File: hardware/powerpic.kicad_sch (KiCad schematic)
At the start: 20 parts, among them U1 PIC16LF1919x-I/MR

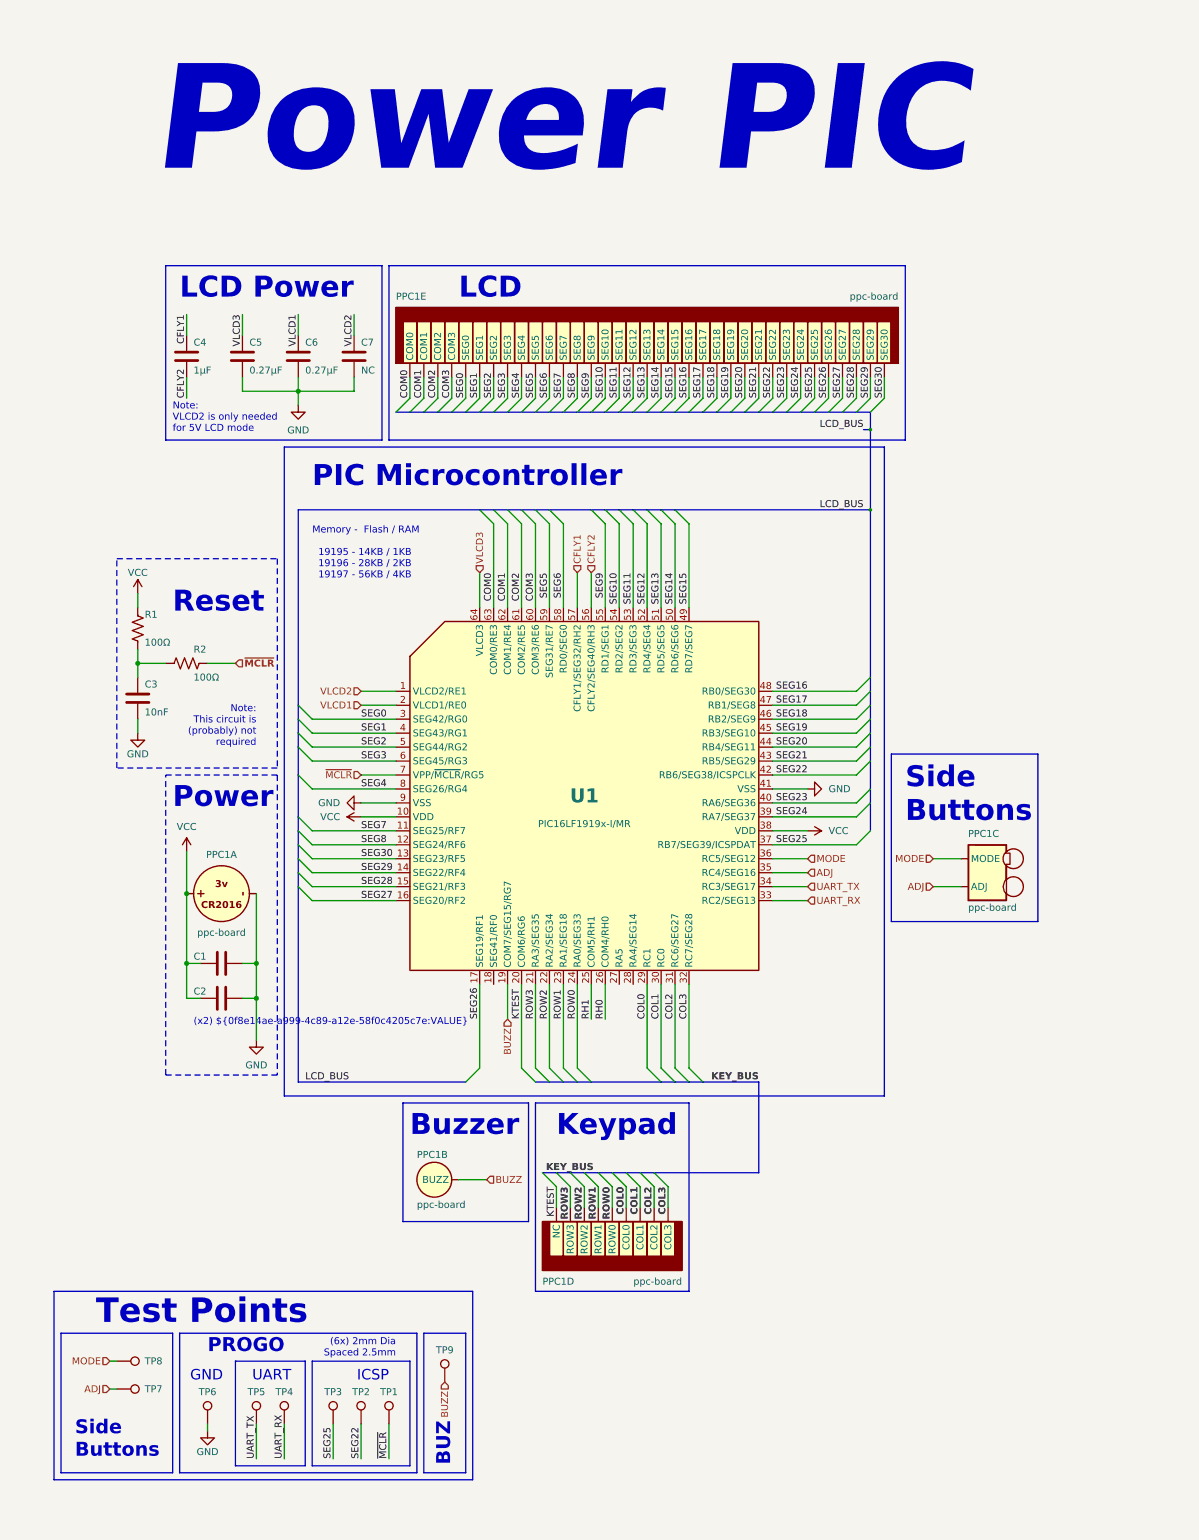
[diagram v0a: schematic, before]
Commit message: Redesigned board with RTCXTAL and led backlight
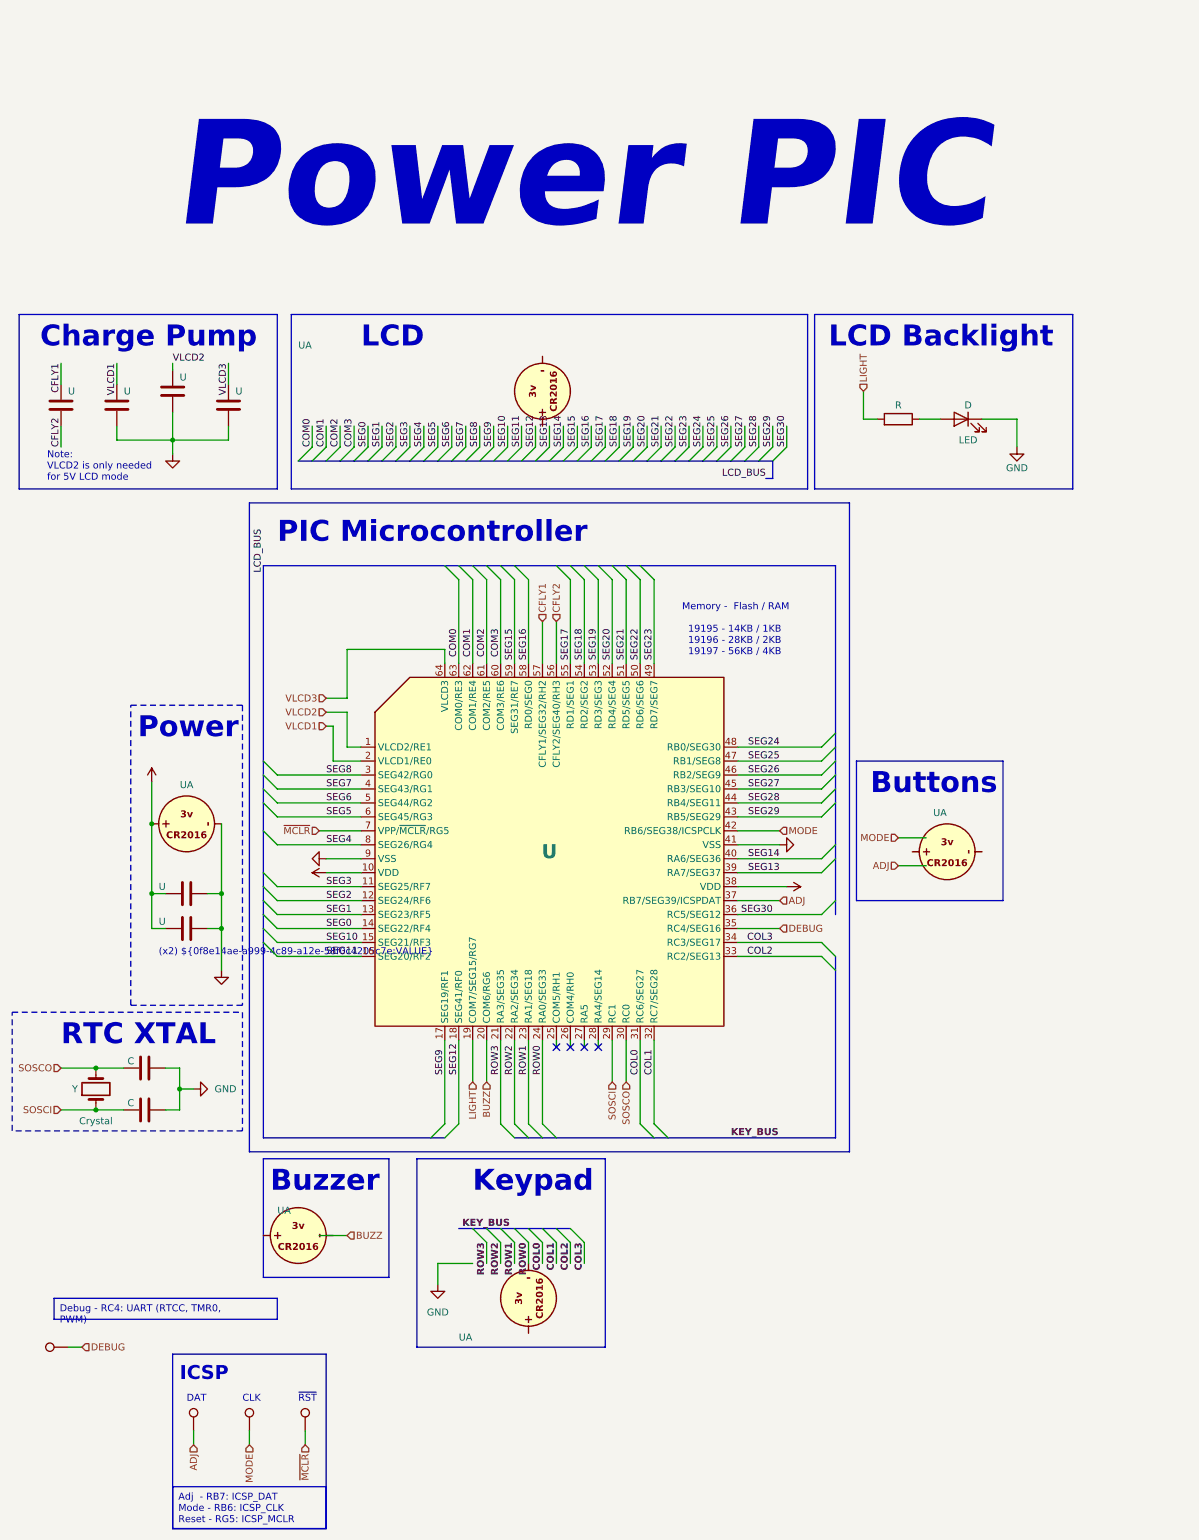
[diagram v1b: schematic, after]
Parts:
- removed C3: 10nF, Capacitor_SMD:C_0402_1005Metric, symbol Device:C
- removed R1, R2: 100Ω, Resistor_SMD:R_0402_1005Metric, symbol Device:R_US
- removed TP1: ~{MCLR}, powerpic:Progo_Pad_D2.0mm, symbol Connector:TestPoint
- removed TP2: ICSP_CLK, powerpic:Progo_Pad_D2.0mm, symbol Connector:TestPoint
- removed TP3: ICSP_DAT, powerpic:Progo_Pad_D2.0mm, symbol Connector:TestPoint
- removed TP4: UART_RX, powerpic:Progo_Pad_D2.0mm, symbol Connector:TestPoint
- removed TP5: UART_TX, powerpic:Progo_Pad_D2.0mm, symbol Connector:TestPoint
- removed TP6: GND, powerpic:Progo_Pad_D2.0mm, symbol Connector:TestPoint
- removed TP7: ADJ, powerpic:Progo_Pad_D2.0mm, symbol Connector:TestPoint
- removed TP8: MODE, powerpic:Progo_Pad_D2.0mm, symbol Connector:TestPoint
- removed TP9: BUZZ, powerpic:Progo_Pad_D2.0mm, symbol Connector:TestPoint
- added C (x2): C, symbol Device:C
- added D: LED, symbol Device:LED
- added R: R, symbol Device:R
- added TP (x4): TestPoint, symbol Connector:TestPoint
- added Y: Crystal, symbol Device:Crystal
- U: renamed from C5; value 0.27μF -> (none); footprint Capacitor_SMD:C_0402_1005Metric -> (none)
- U: renamed from C1; value 0.1μF -> (none); footprint Capacitor_SMD:C_0402_1005Metric -> (none)
- U: renamed from PPC1; value ppc-board -> (none); footprint powerpic:ppc-board -> (none)
- U: renamed from C4; value 1μF -> (none); footprint Capacitor_SMD:C_0402_1005Metric -> (none)
- U: renamed from U1; value PIC16LF1919x-I/MR -> (none); footprint Package_DFN_QFN:QFN-64-1EP_9x9mm_P0.5mm_EP5.4x5.4mm -> (none)
- U: renamed from C7; value NC -> (none); footprint Capacitor_SMD:C_0402_1005Metric -> (none)
- U: renamed from C6; value 0.27μF -> (none); footprint Capacitor_SMD:C_0402_1005Metric -> (none)
- U: renamed from C2; value 0.1μF -> (none); footprint Capacitor_SMD:C_0402_1005Metric -> (none)
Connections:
- net UART_RX is gone; now on net COL2: U.33 (RC2/SEG13)
- net UART_TX is gone; now on net COL3: U.34 (RC3/SEG17)
- net ADJ: now also U.37 (RB7/SEG39/ICSPDAT), TP.1; no longer U.35 (RC4/SEG16), U.5 (ADJ)
- net BUZZ: now also U.20 (COM6/RG6); no longer U.19 (COM7/SEG15/RG7), U.3 (BUZZ)
- net COL0: now also U.31 (RC6/SEG27); no longer U.11 (COL0), U.29 (RC1)
- net COL1: now also U.32 (RC7/SEG28); no longer U.12 (COL1), U.30 (RC0)
- net COL2: no longer U.13 (COL2), U.31 (RC6/SEG27)
- net COL3: no longer U.14 (COL3), U.32 (RC7/SEG28)
- net COM0: no longer U.15 (COM0)
- net COM1: no longer U.16 (COM1)
- net COM2: no longer U.17 (COM2)
- net COM3: no longer U.18 (COM3)
- net GND: now also C.2, C.2, D.1 (K)
- net MODE: now also U.42 (RB6/SEG38/ICSPCLK), TP.1; no longer U.36 (RC5/SEG12), U.4 (MODE)
- net ROW0: now also U.2 (GND); no longer U.10 (ROW0)
- net ROW1: no longer U.9 (ROW1)
- net ROW2: no longer U.8 (ROW2)
- net ROW3: no longer U.7 (ROW3)
- net SEG0: now also U.14 (SEG22/RF4); no longer U.19 (SEG0), U.3 (SEG42/RG0)
- net SEG1: now also U.13 (SEG23/RF5); no longer U.20 (SEG1), U.4 (SEG43/RG1)
- net SEG10: now also U.15 (SEG21/RF3); no longer U.29 (SEG10), U.54 (RD2/SEG2)
- net SEG11: now also U.16 (SEG20/RF2); no longer U.30 (SEG11), U.53 (RD3/SEG3)
- net SEG12: now also U.18 (SEG41/RF0); no longer U.31 (SEG12), U.52 (RD4/SEG4)
- net SEG13: now also U.39 (RA7/SEG37); no longer U.32 (SEG13), U.51 (RD5/SEG5)
- net SEG14: now also U.40 (RA6/SEG36); no longer U.33 (SEG14), U.50 (RD6/SEG6)
- net SEG15: now also U.59 (SEG31/RE7); no longer U.34 (SEG15), U.49 (RD7/SEG7)
- net SEG16: now also U.58 (RD0/SEG0); no longer U.35 (SEG16), U.48 (RB0/SEG30)
- net SEG17: now also U.55 (RD1/SEG1); no longer U.36 (SEG17), U.47 (RB1/SEG8)
- net SEG18: now also U.54 (RD2/SEG2); no longer U.37 (SEG18), U.46 (RB2/SEG9)
- net SEG19: now also U.53 (RD3/SEG3); no longer U.38 (SEG19), U.45 (RB3/SEG10)
- net SEG2: now also U.12 (SEG24/RF6); no longer U.21 (SEG2), U.5 (SEG44/RG2)
- net SEG20: now also U.52 (RD4/SEG4); no longer U.39 (SEG20), U.44 (RB4/SEG11)
- net SEG21: now also U.51 (RD5/SEG5); no longer U.40 (SEG21), U.43 (RB5/SEG29)
- net SEG22: now also U.50 (RD6/SEG6); no longer U.41 (SEG22), U.42 (RB6/SEG38/ICSPCLK)
- net SEG23: now also U.49 (RD7/SEG7); no longer U.40 (RA6/SEG36), U.42 (SEG23)
- net SEG24: now also U.48 (RB0/SEG30); no longer U.39 (RA7/SEG37), U.43 (SEG24)
- net SEG25: now also U.47 (RB1/SEG8); no longer U.37 (RB7/SEG39/ICSPDAT), U.44 (SEG25)
- net SEG26: now also U.46 (RB2/SEG9); no longer U.17 (SEG19/RF1), U.45 (SEG26)
- net SEG27: now also U.45 (RB3/SEG10); no longer U.16 (SEG20/RF2), U.46 (SEG27)
- net SEG28: now also U.44 (RB4/SEG11); no longer U.15 (SEG21/RF3), U.47 (SEG28)
- net SEG29: now also U.43 (RB5/SEG29); no longer U.14 (SEG22/RF4), U.48 (SEG29)
- net SEG3: now also U.11 (SEG25/RF7); no longer U.22 (SEG3), U.6 (SEG45/RG3)
- net SEG30: now also U.36 (RC5/SEG12); no longer U.13 (SEG23/RF5), U.49 (SEG30)
- net SEG4: no longer U.23 (SEG4)
- net SEG5: now also U.6 (SEG45/RG3); no longer U.24 (SEG5), U.59 (SEG31/RE7)
- net SEG6: now also U.5 (SEG44/RG2); no longer U.25 (SEG6), U.58 (RD0/SEG0)
- net SEG7: now also U.4 (SEG43/RG1); no longer U.11 (SEG25/RF7), U.26 (SEG7)
- net SEG8: now also U.3 (SEG42/RG0); no longer U.12 (SEG24/RF6), U.27 (SEG8)
- net SEG9: now also U.17 (SEG19/RF1); no longer U.28 (SEG9), U.55 (RD1/SEG1)
- net ~{MCLR}: now also TP.1
- removed net KTEST: U.20 (COM6/RG6), U.6 (NC)
- net RH0: no longer names the net of U.26 (COM4/RH0)
- net RH1: no longer names the net of U.25 (COM5/RH1)
- new net: D.2 (A), R.1
- new net DEBUG: TP.1, U.35 (RC4/SEG16)
- new net LIGHT: R.2, U.19 (COM7/SEG15/RG7)
- new net SOSCI: C.1, U.29 (RC1), Y.1
- new net SOSCO: C.1, U.30 (RC0), Y.2
- no-connect marks 0 -> 4
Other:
- note added: "Buttons"
- note added: "CLK"
- note added: "Charge Pump"
- note added: "DAT"
- note added: "LCD Backlight"
- note added: "RTC XTAL"
- note added: "~{RST}"
- note removed: "(6x) 2mm Dia Spaced 2.5mm"
- note removed: "BUZ"
- note removed: "GND"
- note removed: "LCD Power"
- note removed: "Note: This circuit is (probably) not required"
- note removed: "PROGO"
- note removed: "Reset"
- note removed: "Side Buttons"
- note removed: "Test Points"
- note removed: "UART"
- moved on the sheet: U, UA

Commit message: Starting work on version 3 of the hardware.
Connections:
- net COM3 is gone; now on net LIGHT: U.60 (COM3/RE6)
- net BUZZ: no longer U.20 (COM6/RG6)
- net LIGHT: no longer U.19 (COM7/SEG15/RG7)
- new net BLE_RX: U.20 (COM6/RG6)
- new net BLE_TX: U.19 (COM7/SEG15/RG7)
- no-connect marks 4 -> 5
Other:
- added sheet BLE_SOC (powerpic-ble.kicad_sch)
- note added: "PowerPIC"
- note added: "TODO"
- note removed: "Note: VLCD2 is only needed for 5V LCD mode"
- note removed: "Power PIC"
- moved on the sheet: C, U, UA, Y

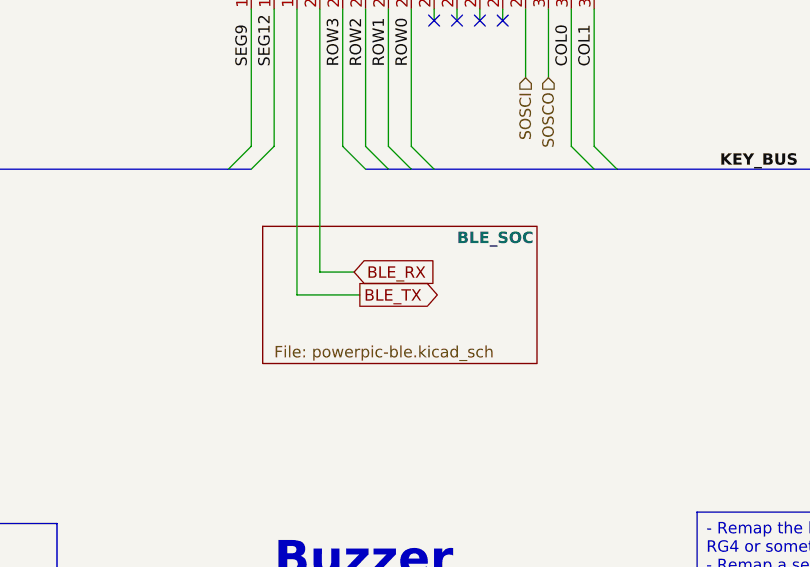
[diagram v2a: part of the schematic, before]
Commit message: hardware: Minor changes. Mostly playing around in the new kicad nightly.
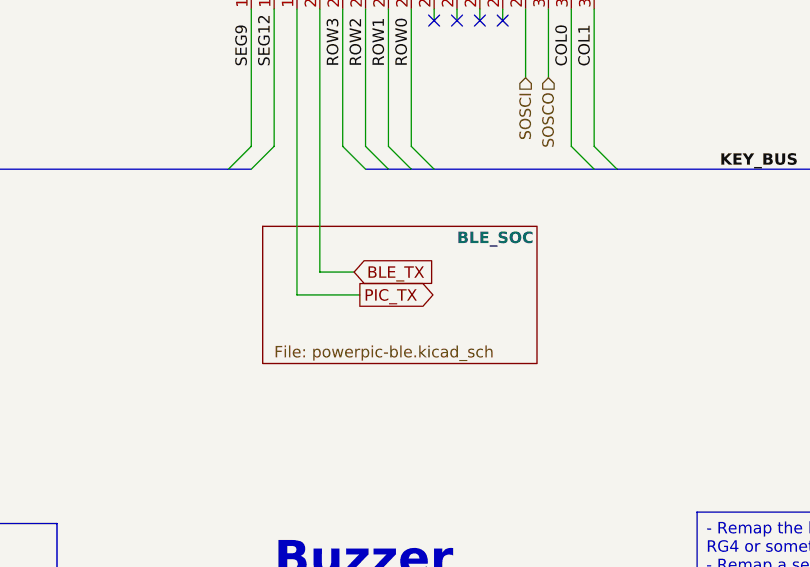
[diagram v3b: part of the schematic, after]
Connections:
- net BLE_RX is gone; now on net BLE_TX: U.20 (COM6/RG6)
- net BLE_TX: no longer U.19 (COM7/SEG15/RG7)
- new net PIC_TX: U.19 (COM7/SEG15/RG7)
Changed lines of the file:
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@@
     (effects (font (size 1.27 1.27)) (justify right bottom))
   )
-  (global_label "BLE_TX" (shape output) (at 98.425 226.06 0) (fields_autoplaced)
+  (global_label "PIC_TX" (shape output) (at 98.425 226.06 0) (fields_autoplaced)
     (effects (font (size 1.27 1.27)) (justify left))
-    (property "Intersheetrefs" "${INTERSHEET_REFS}" (id 0) (at 107.7638 226.06 0)
+    (property "Intersheetrefs" "${INTERSHEET_REFS}" (id 0) (at 107.4615 226.06 0)
       (effects (font (size 1.27 1.27)) (justify left) hide)
     )
   )
-  (global_label "BLE_RX" (shape input) (at 97.79 223.52 0) (fields_autoplaced)
+  (global_label "BLE_TX" (shape input) (at 97.79 223.52 0) (fields_autoplaced)
     (effects (font (size 1.27 1.27)) (justify left))
-    (property "Intersheetrefs" "${INTERSHEET_REFS}" (id 0) (at 107.4312 223.52 0)
+    (property "Intersheetrefs" "${INTERSHEET_REFS}" (id 0) (at 107.1288 223.52 0)
       (effects (font (size 1.27 1.27)) (justify left) hide)
     )
